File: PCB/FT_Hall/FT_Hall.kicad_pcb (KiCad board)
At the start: 2 copper layers, 7.6 x 19.7 mm, 5 parts, among them CON1 Conn_01x03_Pin

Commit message: update pcbs
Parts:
- C1, C2: footprint Capacitor_SMD:C_0805_2012Metric_Pad1.18x1.45mm_HandSolder -> Capacitor_SMD:C_0603_1608Metric
- R1: footprint Resistor_SMD:R_0805_2012Metric_Pad1.20x1.40mm_HandSolder -> Resistor_SMD:R_0603_1608Metric
- moved C2 8.21 mm to (131.6, 76.2), turned to 180 degrees
- moved C1 8.21 mm to (135.1, 76.2), turned to 180 degrees
- moved R1 5.08 mm to (135.9, 73.7)
- moved HAL1 1.27 mm to (133.3, 80.0), turned to -90 degrees
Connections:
- CON1 pad 1: +12V -> /Q
- CON1 pad 3: /Q -> +12V
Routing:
- net /Q: track 15.0 -> 10.6 mm
- net /VS: track 8.91 -> 4.69 mm
- net GND: track 18.6 -> 14.9 mm
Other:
- board size 7.6 x 19.7 mm -> 7.6 x 17.7 mm
- board text added: "Q - +"

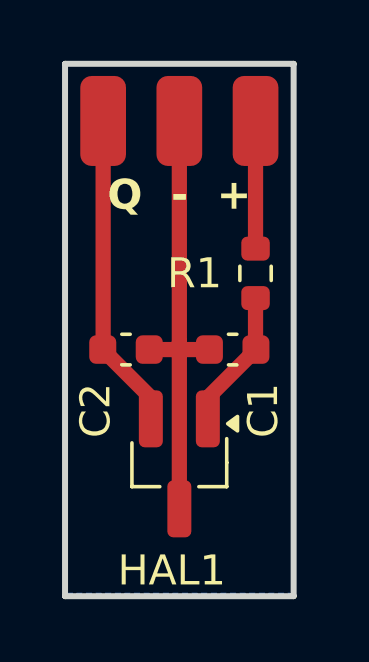
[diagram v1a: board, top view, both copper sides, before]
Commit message: hall and switch done
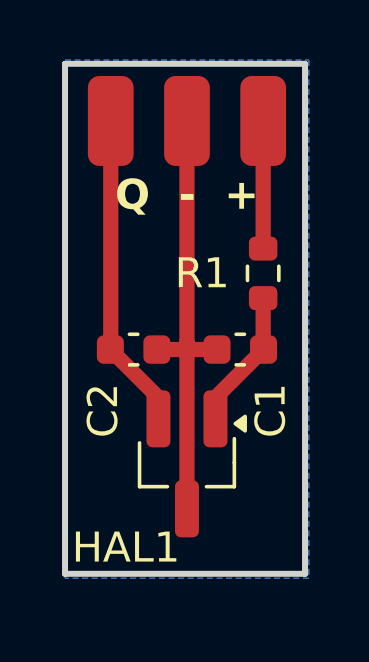
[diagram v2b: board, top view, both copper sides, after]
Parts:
- moved C1 0.25 mm to (135.4, 76.2)
- moved CON1 0.25 mm to (133.6, 68.6)
- moved HAL1 0.25 mm to (133.6, 80.0)
- moved R1 0.25 mm to (136.1, 73.7)
- moved C2 0.25 mm to (131.8, 76.2)
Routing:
- added copper zone on B.Cu, net GND
- removed copper zone on B.Cu, net (none)
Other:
- board size 7.6 x 17.7 mm -> 8 x 17 mm
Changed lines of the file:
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@@
 	(footprint "Resistor_SMD:R_0603_1608Metric"
 		(layer "F.Cu")
-		(at 135.89 73.66 90)
+		(at 136.144 73.66 90)
 		(descr "Resistor SMD 0603 (1608 Metric), square (rectangular) end terminal, IPC_7351 nominal, (Body size source: IPC-SM-782 page 72, https://www.pcb-3d.com/wordpress/wp-content/uploads/ipc-sm-782a_amendment_1_and_2.pdf), generated with kicad-footprint-generator")
 		(tags "resistor")
@@
 	(footprint "Package_TO_SOT_SMD:SOT-23_Handsoldering"
 		(layer "F.Cu")
-		(at 133.35 80.01 -90)
+		(at 133.604 80.01 -90)
 		(descr "SOT-23, Handsoldering")
 		(tags "SOT-23")
 		(property "Reference" "HAL1"
-			(at 3.556 0.254 0)
+			(at 2.794 2.032 0)
 			(layer "F.SilkS")
 			(effects
@@
 	(footprint "Capacitor_SMD:C_0603_1608Metric"
 		(layer "F.Cu")
-		(at 131.572 76.2 180)
+		(at 131.826 76.2 180)
 		(descr "Capacitor SMD 0603 (1608 Metric), square (rectangular) end terminal, IPC_7351 nominal, (Body size source: IPC-SM-782 page 76, https://www.pcb-3d.com/wordpress/wp-content/uploads/ipc-sm-782a_amendment_1_and_2.pdf), generated with kicad-footprint-generator")
 		(tags "capacitor")
@@
 	(footprint "Capacitor_SMD:C_0603_1608Metric"
 		(layer "F.Cu")
-		(at 135.128 76.2 180)
+		(at 135.382 76.2 180)
 		(descr "Capacitor SMD 0603 (1608 Metric), square (rectangular) end terminal, IPC_7351 nominal, (Body size source: IPC-SM-782 page 76, https://www.pcb-3d.com/wordpress/wp-content/uploads/ipc-sm-782a_amendment_1_and_2.pdf), generated with kicad-footprint-generator")
 		(tags "capacitor")
@@
 	(footprint "SMD_3_PADS:3_SMD_PADS"
 		(layer "F.Cu")
-		(at 133.35 68.58)
+		(at 133.604 68.58)
 		(property "Reference" "CON1"
 			(at 0 -0.5 0)
@@
 	(gr_rect
 		(start 129.54 66.675)
-		(end 137.16 84.421)
+		(end 137.54 83.675)
 		(stroke
 			(width 0.2)
@@
 	)
 	(gr_text "Firesport timer\nHall switch\nMartin Vejman\nv1"
-		(at 135.89 68.58 90)
+		(at 136.652 67.564 90)
 		(layer "B.SilkS")
 		(effects
@@
 	)
 	(gr_text "Q  -  +"
-		(at 133.35 71.628 0)
+		(at 133.604 71.628 0)
 		(layer "F.SilkS")
 		(effects
@@
 	)
 	(segment
-		(start 135.89 76.187)
-		(end 135.903 76.2)
+		(start 136.144 76.187)
+		(end 136.157 76.2)
 		(width 0.508)
 		(layer "F.Cu")
@@
 	)
 	(segment
-		(start 135.89 74.485)
-		(end 135.89 76.187)
+		(start 136.144 74.485)
+		(end 136.144 76.187)
 		(width 0.508)
 		(layer "F.Cu")
@@
 	)
 	(segment
-		(start 134.3 77.803)
-		(end 135.903 76.2)
+		(start 134.554 77.803)
+		(end 136.157 76.2)
 		(width 0.508)
 		(layer "F.Cu")
@@
 	)
 	(segment
-		(start 134.3 78.51)
-		(end 134.3 77.803)
+		(start 134.554 78.51)
+		(end 134.554 77.803)
 		(width 0.508)
 		(layer "F.Cu")
@@
 	)
 	(segment
-		(start 132.347 76.2)
-		(end 133.35 76.2)
+		(start 132.601 76.2)
+		(end 133.604 76.2)
 		(width 0.508)
 		(layer "F.Cu")
@@
 	)
 	(segment
-		(start 133.35 76.2)
-		(end 133.35 81.51)
+		(start 133.604 76.2)
+		(end 133.604 81.51)
 		(width 0.508)
 		(layer "F.Cu")
@@
 	)
 	(segment
-		(start 133.35 68.58)
-		(end 133.35 75.946)
+		(start 133.604 68.58)
+		(end 133.604 75.946)
 		(width 0.508)
 		(layer "F.Cu")
@@
 	)
 	(segment
-		(start 134.353 76.2)
-		(end 133.35 76.2)
+		(start 134.607 76.2)
+		(end 133.604 76.2)
 		(width 0.508)
 		(layer "F.Cu")
@@
 	)
 	(segment
-		(start 133.35 75.946)
-		(end 133.35 76.2)
+		(start 133.604 75.946)
+		(end 133.604 76.2)
 		(width 0.508)
 		(layer "F.Cu")
@@
 	)
 	(segment
-		(start 132.4 78.51)
-		(end 132.4 77.803)
+		(start 132.654 78.51)
+		(end 132.654 77.803)
 		(width 0.508)
 		(layer "F.Cu")
@@
 	)
 	(segment
-		(start 130.81 76.187)
-		(end 130.797 76.2)
+		(start 131.064 76.187)
+		(end 131.051 76.2)
 		(width 0.508)
 		(layer "F.Cu")
@@
 	)
 	(segment
-		(start 132.4 77.803)
-		(end 130.797 76.2)
+		(start 132.654 77.803)
+		(end 131.051 76.2)
 		(width 0.508)
 		(layer "F.Cu")
@@
 	)
 	(segment
-		(start 130.81 68.58)
-		(end 130.81 76.187)
+		(start 131.064 68.58)
+		(end 131.064 76.187)
 		(width 0.508)
 		(layer "F.Cu")
@@
 	)
 	(segment
-		(start 135.89 68.58)
-		(end 135.89 72.835)
+		(start 136.144 68.58)
+		(end 136.144 72.835)
 		(width 0.508)
 		(layer "F.Cu")
@@
 	)
 	(zone
-		(net 0)
-		(net_name "")
+		(net 2)
+		(net_name "GND")
 		(layer "B.Cu")
 		(hatch edge 0.5)
@@
 			(thermal_gap 0.5)
 			(thermal_bridge_width 0.5)
-			(island_removal_mode 1)
-			(island_area_min 10)
 		)
 		(polygon
 			(pts
-				(xy 129.54 66.675) (xy 137.16 66.675) (xy 137.16 84.328) (xy 129.54 84.328)
-			)
-		)
+				(xy 129.54 66.548) (xy 137.668 66.548) (xy 137.668 83.82) (xy 129.54 83.82)
+			)
+		)

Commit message: final
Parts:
- HAL1: value ~ -> TLV4906K; footprint Package_TO_SOT_SMD:SOT-23_Handsoldering -> Package_TO_SOT_SMD:SOT-23

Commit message: major changes, production ready
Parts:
- C1, C2: value 4.7nF -> 4.7nF, 25V
- moved CON1 44.7 mm to (104.0, 102.1)
- moved C1 44.7 mm to (105.8, 109.8)
- moved C2 44.7 mm to (102.2, 109.8)
- moved HAL1 44.7 mm to (104.0, 113.6)
- moved R1 44.7 mm to (106.5, 107.2)
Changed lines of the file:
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@@
 			(outputformat 1)
 			(mirror no)
-			(drillshape 1)
+			(drillshape 0)
 			(scaleselection 1)
-			(outputdirectory "")
+			(outputdirectory "Production/Drill/")
 		)
 	)
@@
 	(footprint "Resistor_SMD:R_0603_1608Metric"
 		(layer "F.Cu")
-		(at 136.144 73.66 90)
+		(at 106.54 107.214 90)
 		(descr "Resistor SMD 0603 (1608 Metric), square (rectangular) end terminal, IPC_7351 nominal, (Body size source: IPC-SM-782 page 72, https://www.pcb-3d.com/wordpress/wp-content/uploads/ipc-sm-782a_amendment_1_and_2.pdf), generated with kicad-footprint-generator")
 		(tags "resistor")
@@
 	(footprint "Package_TO_SOT_SMD:SOT-23"
 		(layer "F.Cu")
-		(at 133.604 80.01 -90)
+		(at 104 113.564 -90)
 		(descr "SOT, 3 Pin (https://www.jedec.org/system/files/docs/to-236h.pdf variant AB), generated with kicad-footprint-generator ipc_gullwing_generator.py")
 		(tags "SOT TO_SOT_SMD")
@@
 			)
 		)
-		(property "Datasheet" ""
+		(property "Datasheet" "https://www.lcsc.com/datasheet/lcsc_datasheet_2304140030_Infineon-Technologies-TLV4906K_C126637.pdf"
 			(at 0 0 -90)
 			(unlocked yes)
@@
 			)
 		)
-		(property "Supplier" ""
+		(property "Supplier" "LCSC"
 			(at 0 0 -90)
 			(unlocked yes)
@@
 			)
 		)
-		(property "Supplier no." ""
+		(property "Supplier no." "C126637"
 			(at 0 0 -90)
 			(unlocked yes)
@@
 			)
 		)
-		(property "URL" ""
+		(property "URL" "https://www.lcsc.com/product-detail/Hall-Switches_Infineon-Technologies-TLV4906K_C126637.html"
 			(at 0 0 -90)
 			(unlocked yes)
@@
 	(footprint "Capacitor_SMD:C_0603_1608Metric"
 		(layer "F.Cu")
-		(at 131.826 76.2 180)
+		(at 102.222 109.754 180)
 		(descr "Capacitor SMD 0603 (1608 Metric), square (rectangular) end terminal, IPC_7351 nominal, (Body size source: IPC-SM-782 page 76, https://www.pcb-3d.com/wordpress/wp-content/uploads/ipc-sm-782a_amendment_1_and_2.pdf), generated with kicad-footprint-generator")
 		(tags "capacitor")
@@
 			)
 		)
-		(property "Value" "4.7nF"
+		(property "Value" "4.7nF, 25V"
 			(at 0 1.43 180)
 			(layer "F.Fab")
@@
 			)
 		)
-		(property "Datasheet" ""
+		(property "Datasheet" "https://www.lcsc.com/datasheet/lcsc_datasheet_2304140030_YAGEO-CC0603KRX7R8BB472_C505480.pdf"
 			(at 0 0 180)
 			(unlocked yes)
@@
 			)
 		)
-		(property "Supplier" "PCBWAY"
-			(at 0 0 180)
-			(unlocked yes)
-			(layer "F.Fab")
-			(hide yes)
-			(effects
-				(font
-					(size 1 1)
-					(thickness 0.15)
-				)
-			)
-		)
-		(property "Supplier no." ""
-			(at 0 0 180)
-			(unlocked yes)
-			(layer "F.Fab")
-			(hide yes)
-			(effects
-				(font
-					(size 1 1)
-					(thickness 0.15)
-				)
-			)
-		)
-		(property "URL" ""
+		(property "Supplier" "LCSC"
+			(at 0 0 180)
+			(unlocked yes)
+			(layer "F.Fab")
+			(hide yes)
+			(effects
+				(font
+					(size 1 1)
+					(thickness 0.15)
+				)
+			)
+		)
+		(property "Supplier no." "C505480"
+			(at 0 0 180)
+			(unlocked yes)
+			(layer "F.Fab")
+			(hide yes)
+			(effects
+				(font
+					(size 1 1)
+					(thickness 0.15)
+				)
+			)
+		)
+		(property "URL" "https://www.lcsc.com/product-detail/Multilayer-Ceramic-Capacitors-MLCC-SMD-SMT_YAGEO-CC0603KRX7R8BB472_C505480.html"
 			(at 0 0 180)
 			(unlocked yes)
@@
 	(footprint "Capacitor_SMD:C_0603_1608Metric"
 		(layer "F.Cu")
-		(at 135.382 76.2 180)
+		(at 105.778 109.754 180)
 		(descr "Capacitor SMD 0603 (1608 Metric), square (rectangular) end terminal, IPC_7351 nominal, (Body size source: IPC-SM-782 page 76, https://www.pcb-3d.com/wordpress/wp-content/uploads/ipc-sm-782a_amendment_1_and_2.pdf), generated with kicad-footprint-generator")
 		(tags "capacitor")
@@
 			)
 		)
-		(property "Value" "4.7nF"
+		(property "Value" "4.7nF, 25V"
 			(at 0 1.43 180)
 			(layer "F.Fab")
@@
 			)
 		)
-		(property "Datasheet" ""
+		(property "Datasheet" "https://www.lcsc.com/datasheet/lcsc_datasheet_2304140030_YAGEO-CC0603KRX7R8BB472_C505480.pdf"
 			(at 0 0 180)
 			(unlocked yes)
@@
 			)
 		)
-		(property "Supplier" "PCBWAY"
-			(at 0 0 180)
-			(unlocked yes)
-			(layer "F.Fab")
-			(hide yes)
-			(effects
-				(font
-					(size 1 1)
-					(thickness 0.15)
-				)
-			)
-		)
-		(property "Supplier no." ""
-			(at 0 0 180)
-			(unlocked yes)
-			(layer "F.Fab")
-			(hide yes)
-			(effects
-				(font
-					(size 1 1)
-					(thickness 0.15)
-				)
-			)
-		)
-		(property "URL" ""
+		(property "Supplier" "LCSC"
+			(at 0 0 180)
+			(unlocked yes)
+			(layer "F.Fab")
+			(hide yes)
+			(effects
+				(font
+					(size 1 1)
+					(thickness 0.15)
+				)
+			)
+		)
+		(property "Supplier no." "C505480"
+			(at 0 0 180)
+			(unlocked yes)
+			(layer "F.Fab")
+			(hide yes)
+			(effects
+				(font
+					(size 1 1)
+					(thickness 0.15)
+				)
+			)
+		)
+		(property "URL" "https://www.lcsc.com/product-detail/Multilayer-Ceramic-Capacitors-MLCC-SMD-SMT_YAGEO-CC0603KRX7R8BB472_C505480.html"
 			(at 0 0 180)
 			(unlocked yes)
@@
 	(footprint "SMD_3_PADS:3_SMD_PADS"
 		(layer "F.Cu")
-		(at 133.604 68.58)
+		(at 104 102.134)
 		(property "Reference" "CON1"
 			(at 0 -0.5 0)
@@
 	)
 	(gr_rect
-		(start 129.54 66.675)
-		(end 137.54 83.675)
+		(start 100 100)
+		(end 108 117)
 		(stroke
-			(width 0.2)
+			(width 0.05)
 			(type default)
 		)
@@
 	)
 	(gr_text "Firesport timer\nHall switch\nMartin Vejman\nv1"
-		(at 136.652 67.564 90)
+		(at 107.048 101.118 90)
 		(layer "B.SilkS")
 		(effects
@@
 	)
 	(gr_text "Q  -  +"
-		(at 133.604 71.628 0)
+		(at 104 105.182 0)
 		(layer "F.SilkS")
 		(effects
@@
 	)
 	(segment
-		(start 136.144 76.187)
-		(end 136.157 76.2)
+		(start 106.54 109.741)
+		(end 106.553 109.754)
 		(width 0.508)
 		(layer "F.Cu")
@@
 	)
 	(segment
-		(start 136.144 74.485)
-		(end 136.144 76.187)
+		(start 106.54 108.039)
+		(end 106.54 109.741)
 		(width 0.508)
 		(layer "F.Cu")
@@
 	)
 	(segment
-		(start 134.554 77.803)
-		(end 136.157 76.2)
+		(start 104.95 111.357)
+		(end 106.553 109.754)
 		(width 0.508)
 		(layer "F.Cu")
@@
 	)
 	(segment
-		(start 134.554 78.51)
-		(end 134.554 77.803)
+		(start 104.95 112.064)
+		(end 104.95 111.357)
 		(width 0.508)
 		(layer "F.Cu")
@@
 	)
 	(segment
-		(start 132.601 76.2)
-		(end 133.604 76.2)
+		(start 102.997 109.754)
+		(end 104 109.754)
 		(width 0.508)
 		(layer "F.Cu")
@@
 	)
 	(segment
-		(start 133.604 76.2)
-		(end 133.604 81.51)
+		(start 104 109.754)
+		(end 104 115.064)
 		(width 0.508)
 		(layer "F.Cu")
@@
 	)
 	(segment
-		(start 133.604 68.58)
-		(end 133.604 75.946)
+		(start 104 102.134)
+		(end 104 109.5)
 		(width 0.508)
 		(layer "F.Cu")
@@
 	)
 	(segment
-		(start 134.607 76.2)
-		(end 133.604 76.2)
+		(start 105.003 109.754)
+		(end 104 109.754)
 		(width 0.508)
 		(layer "F.Cu")
@@
 	)
 	(segment
-		(start 133.604 75.946)
-		(end 133.604 76.2)
+		(start 104 109.5)
+		(end 104 109.754)
 		(width 0.508)
 		(layer "F.Cu")
@@
 	)
 	(segment
-		(start 132.654 78.51)
-		(end 132.654 77.803)
+		(start 103.05 112.064)
+		(end 103.05 111.357)
 		(width 0.508)
 		(layer "F.Cu")
@@
 	)
 	(segment
-		(start 131.064 76.187)
-		(end 131.051 76.2)
+		(start 101.46 109.741)
+		(end 101.447 109.754)
 		(width 0.508)
 		(layer "F.Cu")
@@
 	)
 	(segment
-		(start 132.654 77.803)
-		(end 131.051 76.2)
+		(start 103.05 111.357)
+		(end 101.447 109.754)
 		(width 0.508)
 		(layer "F.Cu")
@@
 	)
 	(segment
-		(start 131.064 68.58)
-		(end 131.064 76.187)
+		(start 101.46 102.134)
+		(end 101.46 109.741)
 		(width 0.508)
 		(layer "F.Cu")
@@
 	)
 	(segment
-		(start 136.144 68.58)
-		(end 136.144 72.835)
+		(start 106.54 102.134)
+		(end 106.54 106.389)
 		(width 0.508)
 		(layer "F.Cu")
@@
 		(polygon
 			(pts
-				(xy 129.54 66.548) (xy 137.668 66.548) (xy 137.668 83.82) (xy 129.54 83.82)
-			)
-		)
+				(xy 100 100) (xy 108 100) (xy 108 117) (xy 100 117)
+			)
+		)

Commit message: panelization
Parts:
- renumbered C1 to C101, C2 to C102, CON1 to CON101, HAL1 to Q101, R1 to R101
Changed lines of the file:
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@@
 		(descr "Resistor SMD 0603 (1608 Metric), square (rectangular) end terminal, IPC_7351 nominal, (Body size source: IPC-SM-782 page 72, https://www.pcb-3d.com/wordpress/wp-content/uploads/ipc-sm-782a_amendment_1_and_2.pdf), generated with kicad-footprint-generator")
 		(tags "resistor")
-		(property "Reference" "R1"
+		(property "Reference" "R101"
 			(at 0 -2.032 180)
 			(layer "F.SilkS")
+			(hide yes)
 			(effects
 				(font
@@
 		)
 		(property "URL" ""
+			(at 0 0 90)
+			(unlocked yes)
+			(layer "F.Fab")
+			(hide yes)
+			(effects
+				(font
+					(size 1 1)
+					(thickness 0.15)
+				)
+			)
+		)
+		(property "Accept alternative part" ""
 			(at 0 0 90)
 			(unlocked yes)
@@
 		(descr "SOT, 3 Pin (https://www.jedec.org/system/files/docs/to-236h.pdf variant AB), generated with kicad-footprint-generator ipc_gullwing_generator.py")
 		(tags "SOT TO_SOT_SMD")
-		(property "Reference" "HAL1"
+		(property "Reference" "Q101"
 			(at 2.74 2.104 180)
 			(layer "F.SilkS")
+			(hide yes)
 			(effects
 				(font
@@
 		)
 		(property "URL" "https://www.lcsc.com/product-detail/Hall-Switches_Infineon-Technologies-TLV4906K_C126637.html"
+			(at 0 0 -90)
+			(unlocked yes)
+			(layer "F.Fab")
+			(hide yes)
+			(effects
+				(font
+					(size 1 1)
+					(thickness 0.15)
+				)
+			)
+		)
+		(property "Accept alternative part" "NO"
 			(at 0 0 -90)
 			(unlocked yes)
@@
 		(descr "Capacitor SMD 0603 (1608 Metric), square (rectangular) end terminal, IPC_7351 nominal, (Body size source: IPC-SM-782 page 76, https://www.pcb-3d.com/wordpress/wp-content/uploads/ipc-sm-782a_amendment_1_and_2.pdf), generated with kicad-footprint-generator")
 		(tags "capacitor")
-		(property "Reference" "C2"
+		(property "Reference" "C102"
 			(at 1.016 -2.032 90)
 			(layer "F.SilkS")
+			(hide yes)
 			(effects
 				(font
@@
 			)
 		)
-		(property "Datasheet" "https://www.lcsc.com/datasheet/lcsc_datasheet_2304140030_YAGEO-CC0603KRX7R8BB472_C505480.pdf"
+		(property "Datasheet" ""
 			(at 0 0 180)
 			(unlocked yes)
@@
 			)
 		)
-		(property "Supplier" "LCSC"
-			(at 0 0 180)
-			(unlocked yes)
-			(layer "F.Fab")
-			(hide yes)
-			(effects
-				(font
-					(size 1 1)
-					(thickness 0.15)
-				)
-			)
-		)
-		(property "Supplier no." "C505480"
-			(at 0 0 180)
-			(unlocked yes)
-			(layer "F.Fab")
-			(hide yes)
-			(effects
-				(font
-					(size 1 1)
-					(thickness 0.15)
-				)
-			)
-		)
-		(property "URL" "https://www.lcsc.com/product-detail/Multilayer-Ceramic-Capacitors-MLCC-SMD-SMT_YAGEO-CC0603KRX7R8BB472_C505480.html"
+		(property "Supplier" "PCBWAY"
+			(at 0 0 180)
+			(unlocked yes)
+			(layer "F.Fab")
+			(hide yes)
+			(effects
+				(font
+					(size 1 1)
+					(thickness 0.15)
+				)
+			)
+		)
+		(property "Supplier no." ""
+			(at 0 0 180)
+			(unlocked yes)
+			(layer "F.Fab")
+			(hide yes)
+			(effects
+				(font
+					(size 1 1)
+					(thickness 0.15)
+				)
+			)
+		)
+		(property "URL" ""
+			(at 0 0 180)
+			(unlocked yes)
+			(layer "F.Fab")
+			(hide yes)
+			(effects
+				(font
+					(size 1 1)
+					(thickness 0.15)
+				)
+			)
+		)
+		(property "Accept alternative part" ""
 			(at 0 0 180)
 			(unlocked yes)
@@
 		(descr "Capacitor SMD 0603 (1608 Metric), square (rectangular) end terminal, IPC_7351 nominal, (Body size source: IPC-SM-782 page 76, https://www.pcb-3d.com/wordpress/wp-content/uploads/ipc-sm-782a_amendment_1_and_2.pdf), generated with kicad-footprint-generator")
 		(tags "capacitor")
-		(property "Reference" "C1"
+		(property "Reference" "C101"
 			(at -1.016 -2.032 -90)
 			(layer "F.SilkS")
+			(hide yes)
 			(effects
 				(font
@@
 			)
 		)
-		(property "Datasheet" "https://www.lcsc.com/datasheet/lcsc_datasheet_2304140030_YAGEO-CC0603KRX7R8BB472_C505480.pdf"
+		(property "Datasheet" ""
 			(at 0 0 180)
 			(unlocked yes)
@@
 			)
 		)
-		(property "Supplier" "LCSC"
-			(at 0 0 180)
-			(unlocked yes)
-			(layer "F.Fab")
-			(hide yes)
-			(effects
-				(font
-					(size 1 1)
-					(thickness 0.15)
-				)
-			)
-		)
-		(property "Supplier no." "C505480"
-			(at 0 0 180)
-			(unlocked yes)
-			(layer "F.Fab")
-			(hide yes)
-			(effects
-				(font
-					(size 1 1)
-					(thickness 0.15)
-				)
-			)
-		)
-		(property "URL" "https://www.lcsc.com/product-detail/Multilayer-Ceramic-Capacitors-MLCC-SMD-SMT_YAGEO-CC0603KRX7R8BB472_C505480.html"
+		(property "Supplier" "PCBWAY"
+			(at 0 0 180)
+			(unlocked yes)
+			(layer "F.Fab")
+			(hide yes)
+			(effects
+				(font
+					(size 1 1)
+					(thickness 0.15)
+				)
+			)
+		)
+		(property "Supplier no." ""
+			(at 0 0 180)
+			(unlocked yes)
+			(layer "F.Fab")
+			(hide yes)
+			(effects
+				(font
+					(size 1 1)
+					(thickness 0.15)
+				)
+			)
+		)
+		(property "URL" ""
+			(at 0 0 180)
+			(unlocked yes)
+			(layer "F.Fab")
+			(hide yes)
+			(effects
+				(font
+					(size 1 1)
+					(thickness 0.15)
+				)
+			)
+		)
+		(property "Accept alternative part" ""
 			(at 0 0 180)
 			(unlocked yes)
@@
 		(layer "F.Cu")
 		(at 104 102.134)
-		(property "Reference" "CON1"
+		(property "Reference" "CON101"
 			(at 0 -0.5 0)
 			(unlocked yes)
@@
 			(at 0 0 0)
 			(unlocked yes)
+			(layer "F.Fab")
+			(hide yes)
+			(effects
+				(font
+					(size 1 1)
+					(thickness 0.15)
+				)
+			)
+		)
+		(property "Accept alternative part" ""
+			(at 0 0 0)
+			(unlocked yes)
